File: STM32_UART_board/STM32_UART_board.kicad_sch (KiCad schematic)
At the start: 21 parts, among them J1 SWD, J2 Scooter, J4 Conn_01x10, J5 Conn_01x10, SW1 SW_Push, U1 LM2574HVM-5, U3 AMS1117-3.3, U4 STM32C011J6Mx, U5 STM32C011F6Px

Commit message: schematic mostly done
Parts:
- removed D2, D3: D, symbol Device:D
- added C2: 100n, Capacitor_SMD:C_0603_1608Metric_Pad1.08x0.95mm_HandSolder, symbol Device:C
- added Q1: AO4612_C4748739, easyeda2kicad:SOIC-8_L4.9-W3.9-P1.27-LS6.0-BL-2, symbol easyeda2kicad:AO4612_C4748739
- added R1, R3: 100k, symbol Device:R
- added U1: BAS70-05, easyeda2kicad:SOT-23-3_L2.9-W1.3-P1.90-LS2.4-BR, symbol easyeda2kicad:BAS70-05_C7461133
- H1, H2, H3, H4: value ~ -> MountingHole; footprint MountingHole:MountingHole_3.2mm_M3_DIN965_Pad -> MountingHole:MountingHole_3.2mm_M3; now in the parts list
- R2: value R -> 300k; footprint Resistor_SMD:R_0603_1608Metric -> (none)
- SW1: footprint Connector_PinHeader_2.54mm:PinHeader_1x02_P2.54mm_Vertical -> (none)
- U5: renamed from U4; now not fitted; now left out of the parts list
- renumbered C2 to C3, C3 to C4, J4 to J3, J5 to J4, U1 to U2, U5 to U4
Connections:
- net +3.3V: no longer J2.5 (Pin_5), J4.7 (Pin_7), R2.2, U4.17 (PA10/PA12), U5.6 (PA10/PA12)
- net BUTTON: now also U1.2; no longer SW1.1
- net GND: now also U2.5 (~{ON}/OFF), Q1.1 (S2), R3.2
- net PIN_15: now also Q1.2 (G2), R3.1; no longer U2.5 (~{ON}/OFF)
- net VCC: no longer C1.1, U2.10 (VIN)
- net Q1_G1: now reaches R2.1
- net Q1_G1: now also C2.2, Q1.4 (G1), R1.2
- new net: SW1.1, U1.3
- new net +36V: C1.1, Q1.5 (D1), Q1.6 (D1), U2.10 (VIN)
- new net BATT+: C2.1, Q1.3 (S1), R1.1
- new net EN: J2.5 (Pin_5), J4.7 (Pin_7), U4.17 (PA10/PA12), U5.6 (PA10/PA12)
- new net Q1_D2: Q1.7 (D2), Q1.8 (D2), R2.2, U1.1
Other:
- note added: "G1,S1,D1 -> P-MOS"
- note added: "G2,S2,D2 -> N-MOS"
- note added: "M3 holes"
- note removed: "open-drain uC pin"
- moved on the sheet: J1, J2, J3, J4, U4

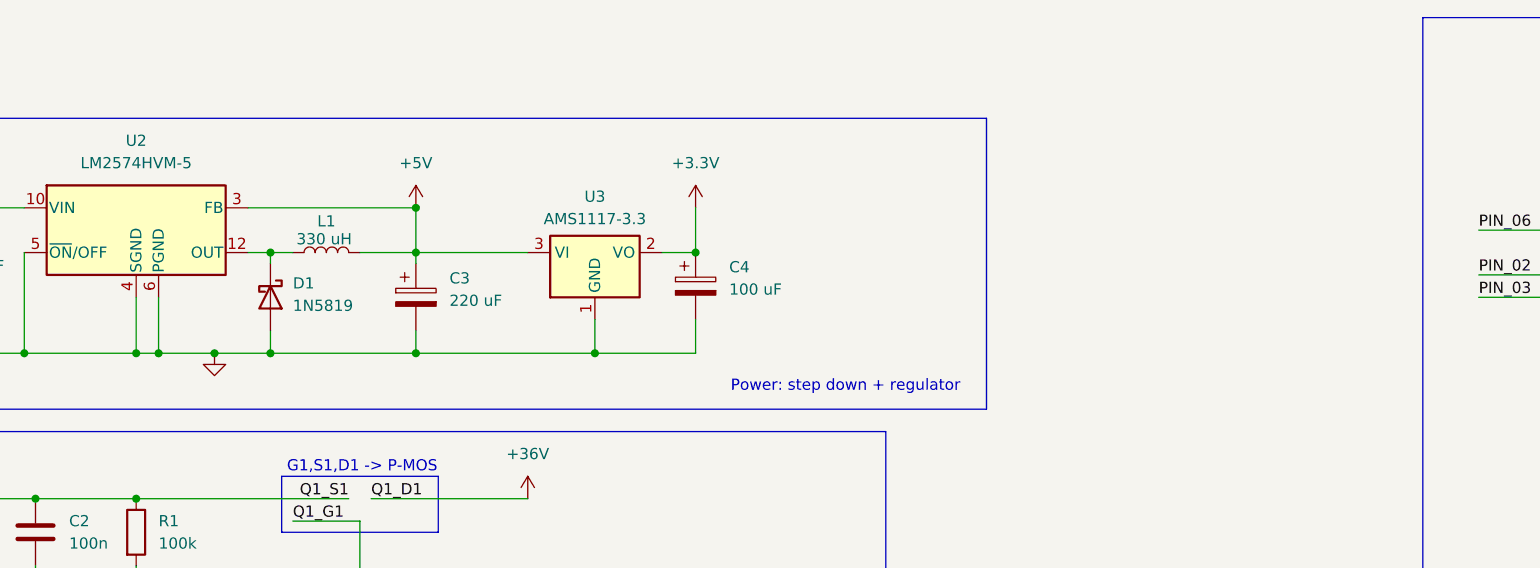
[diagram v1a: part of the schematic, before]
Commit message: added footprints
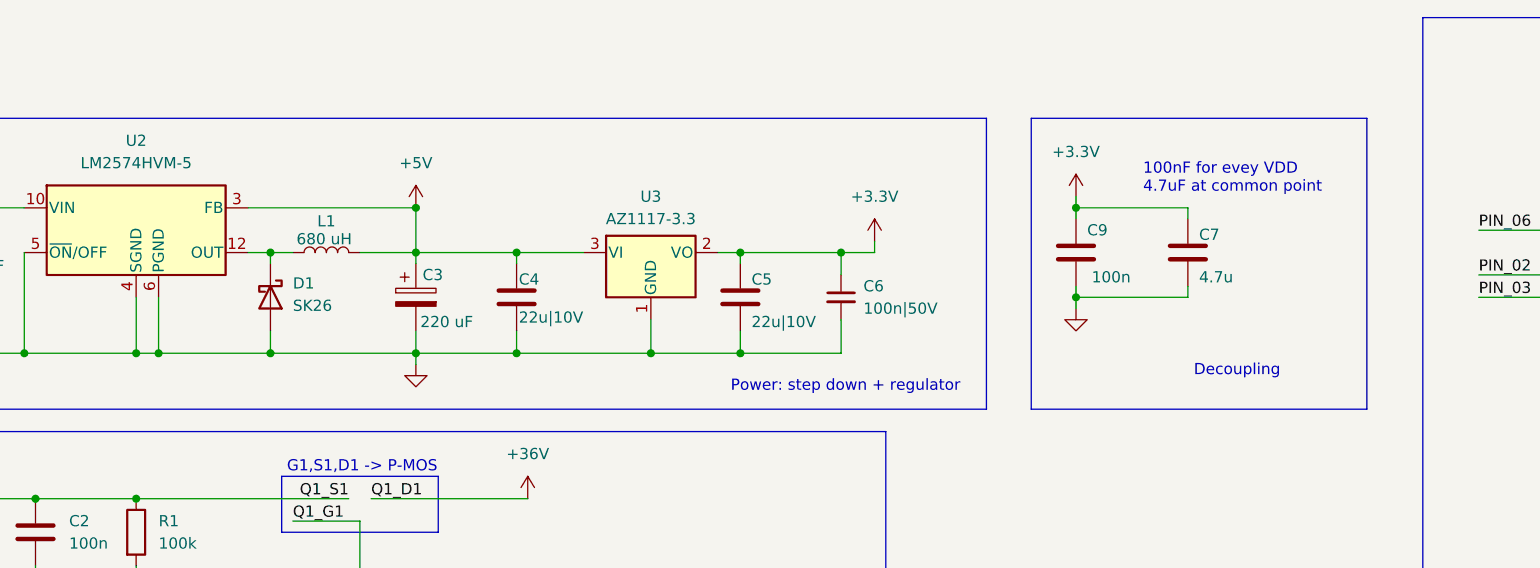
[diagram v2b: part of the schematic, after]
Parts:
- removed C4: 100 uF, symbol Device:C_Polarized
- removed U3: AMS1117-3.3, Package_TO_SOT_SMD:SOT-223-3_TabPin2, symbol Regulator_Linear:AMS1117-3.3
- added C4, C5: 22u|10V, Capacitor_SMD:C_0805_2012Metric_Pad1.18x1.45mm_HandSolder, symbol Device:C
- added C6: 100n|50V, Capacitor_SMD:C_0603_1608Metric_Pad1.08x0.95mm_HandSolder, symbol Device:C_Small
- added C7: 4.7u, Capacitor_SMD:C_0805_2012Metric_Pad1.18x1.45mm_HandSolder, symbol Device:C
- added C9: 100n, Capacitor_SMD:C_0603_1608Metric_Pad1.08x0.95mm_HandSolder, symbol Device:C
- added U3: AZ1117-3.3, Package_TO_SOT_SMD:SOT-223-3_TabPin2, symbol Regulator_Linear:AZ1117-3.3
- C1: footprint (none) -> Capacitor_SMD:CP_Elec_6.3x7.7; Shop (none) -> https://www.tme.eu/pl/details/gsc00bm2201jarl/kondensatory-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
- C3: footprint (none) -> Capacitor_SMD:CP_Elec_8x10
- D1: value 1N5819 -> SK26; footprint (none) -> Diode_SMD:D_SMB_Handsoldering; Shop (none) -> https://www.tme.eu/pl/en/details/sk26-dio/smd-schottky-diod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
- L1: value 330 uH -> 680 uH; footprint Inductor_SMD:L_7.3x7.3_H4.5 -> Inductor_SMD:L_12x12mm_H8mm
- Q1: Shop (none) -> https://www.tme.eu/pl/details/ao4611/tranzystory-multikanal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
- U1: Shop (none) -> https://www.tme.eu/pl/en/details/bas70-05-dio/smd-schottky-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
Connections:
- net +3.3V: now also C5.1, C6.1, C7.1, C9.1, U3.2 (VO)
- net +5V: now also C4.1, U3.3 (VI)
- net GND: now also C4.2, C5.2, C6.2, C7.2, C9.2, U3.1 (GND)
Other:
- note added: "100nF for evey VDD 4.7uF at common point"
- note added: "Decoupling"
